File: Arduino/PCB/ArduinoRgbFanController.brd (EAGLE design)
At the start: 100 x 100 mm, 53 parts, among them IC2 ARDUINO_MKRFOX1200PROTOPADS, Q1 MOSFET-PCHANNEL, Q2 MOSFET-NCHANNELAO3404A

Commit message: Tidied up schematic.
Added values to resistors.
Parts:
- R10, R7, R8, R9: value (none) -> 10k
- R2, R20, R3, R4, R6: value (none) -> 100k
- R21: value (none) -> 10R
- R28: value (none) -> 300R
- R5: value (none) -> 00k
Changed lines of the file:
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@@
 </element>
 <element name="IC2" library="Arduino" package="ARDUINO_MKRFOX1200_PROTOPADS" value="ARDUINO_MKRFOX1200PROTOPADS" x="37.465" y="30.7975"/>
-<element name="R28" library="SparkFun-Resistors" package="1206" value="" x="81.5975" y="56.515" smashed="yes" rot="R180">
+<element name="R28" library="SparkFun-Resistors" package="1206" value="300R" x="81.5975" y="56.515" smashed="yes" rot="R180">
 <attribute name="VALUE" x="82.9945" y="58.039" size="0.4064" layer="27" rot="R180"/>
 </element>
@@
 <attribute name="VALUE" x="91.821" y="11.6205" size="0.4064" layer="27" rot="R180"/>
 </element>
-<element name="R20" library="SparkFun-Resistors" package="1206" value="" x="86.36" y="10.795" smashed="yes" rot="R90">
+<element name="R20" library="SparkFun-Resistors" package="1206" value="100k" x="86.36" y="10.795" smashed="yes" rot="R90">
 <attribute name="NAME" x="85.4075" y="13.5255" size="1.016" layer="25"/>
 <attribute name="VALUE" x="87.884" y="9.398" size="0.4064" layer="27" rot="R90"/>
 </element>
-<element name="R21" library="SparkFun-Resistors" package="1206" value="" x="95.885" y="11.43" smashed="yes">
+<element name="R21" library="SparkFun-Resistors" package="1206" value="10R" x="95.885" y="11.43" smashed="yes">
 <attribute name="NAME" x="95.25" y="12.8905" size="1.016" layer="25"/>
 <attribute name="VALUE" x="94.488" y="9.906" size="0.4064" layer="27"/>
@@
 <attribute name="VALUE" x="15.875" y="51.435" size="1.27" layer="27" rot="R270"/>
 </element>
-<element name="R2" library="SparkFun-Resistors" package="1206" value="" x="15.24" y="43.18" smashed="yes" rot="R180">
+<element name="R2" library="SparkFun-Resistors" package="1206" value="100k" x="15.24" y="43.18" smashed="yes" rot="R180">
 <attribute name="NAME" x="13.0175" y="44.6405" size="1.016" layer="25"/>
 <attribute name="VALUE" x="16.637" y="44.704" size="0.4064" layer="27" rot="R180"/>
 </element>
-<element name="R3" library="SparkFun-Resistors" package="1206" value="" x="15.24" y="27.94" smashed="yes" rot="R180">
+<element name="R3" library="SparkFun-Resistors" package="1206" value="100k" x="15.24" y="27.94" smashed="yes" rot="R180">
 <attribute name="NAME" x="13.0175" y="29.4005" size="1.016" layer="25"/>
 <attribute name="VALUE" x="16.637" y="29.464" size="0.4064" layer="27" rot="R180"/>
 </element>
-<element name="R4" library="SparkFun-Resistors" package="1206" value="" x="85.725" y="46.99" smashed="yes">
+<element name="R4" library="SparkFun-Resistors" package="1206" value="100k" x="85.725" y="46.99" smashed="yes">
 <attribute name="NAME" x="84.455" y="48.133" size="1.016" layer="25"/>
 <attribute name="VALUE" x="84.328" y="45.466" size="0.4064" layer="27"/>
 </element>
-<element name="R5" library="SparkFun-Resistors" package="1206" value="" x="85.725" y="25.4" smashed="yes">
+<element name="R5" library="SparkFun-Resistors" package="1206" value="00k" x="85.725" y="25.4" smashed="yes">
 <attribute name="NAME" x="83.5025" y="26.8605" size="1.016" layer="25"/>
 <attribute name="VALUE" x="84.328" y="23.876" size="0.4064" layer="27"/>
 </element>
-<element name="R6" library="SparkFun-Resistors" package="1206" value="" x="75.565" y="10.795" smashed="yes" rot="R270">
+<element name="R6" library="SparkFun-Resistors" package="1206" value="100k" x="75.565" y="10.795" smashed="yes" rot="R270">
 <attribute name="NAME" x="74.6125" y="7.1755" size="1.016" layer="25"/>
 <attribute name="VALUE" x="74.041" y="12.192" size="0.4064" layer="27" rot="R270"/>
 </element>
-<element name="R7" library="SparkFun-Resistors" package="1206" value="" x="85.725" y="32.385" smashed="yes" rot="R180">
+<element name="R7" library="SparkFun-Resistors" package="1206" value="10k" x="85.725" y="32.385" smashed="yes" rot="R180">
 <attribute name="NAME" x="83.82" y="34.163" size="1.016" layer="25"/>
 <attribute name="VALUE" x="87.122" y="33.909" size="0.4064" layer="27" rot="R180"/>
 </element>
-<element name="R8" library="SparkFun-Resistors" package="1206" value="" x="85.725" y="37.465" smashed="yes" rot="R180">
+<element name="R8" library="SparkFun-Resistors" package="1206" value="10k" x="85.725" y="37.465" smashed="yes" rot="R180">
 <attribute name="NAME" x="83.5025" y="38.9255" size="1.016" layer="25"/>
 <attribute name="VALUE" x="87.122" y="38.989" size="0.4064" layer="27" rot="R180"/>
 </element>
-<element name="R9" library="SparkFun-Resistors" package="1206" value="" x="15.24" y="20.32" smashed="yes">
+<element name="R9" library="SparkFun-Resistors" package="1206" value="10k" x="15.24" y="20.32" smashed="yes">
 <attribute name="NAME" x="13.0175" y="21.7805" size="1.016" layer="25"/>
 <attribute name="VALUE" x="13.843" y="18.796" size="0.4064" layer="27"/>
 </element>
-<element name="R10" library="SparkFun-Resistors" package="1206" value="" x="15.24" y="34.925" smashed="yes">
+<element name="R10" library="SparkFun-Resistors" package="1206" value="10k" x="15.24" y="34.925" smashed="yes">
 <attribute name="NAME" x="13.0175" y="36.3855" size="1.016" layer="25"/>
 <attribute name="VALUE" x="13.843" y="33.401" size="0.4064" layer="27"/>

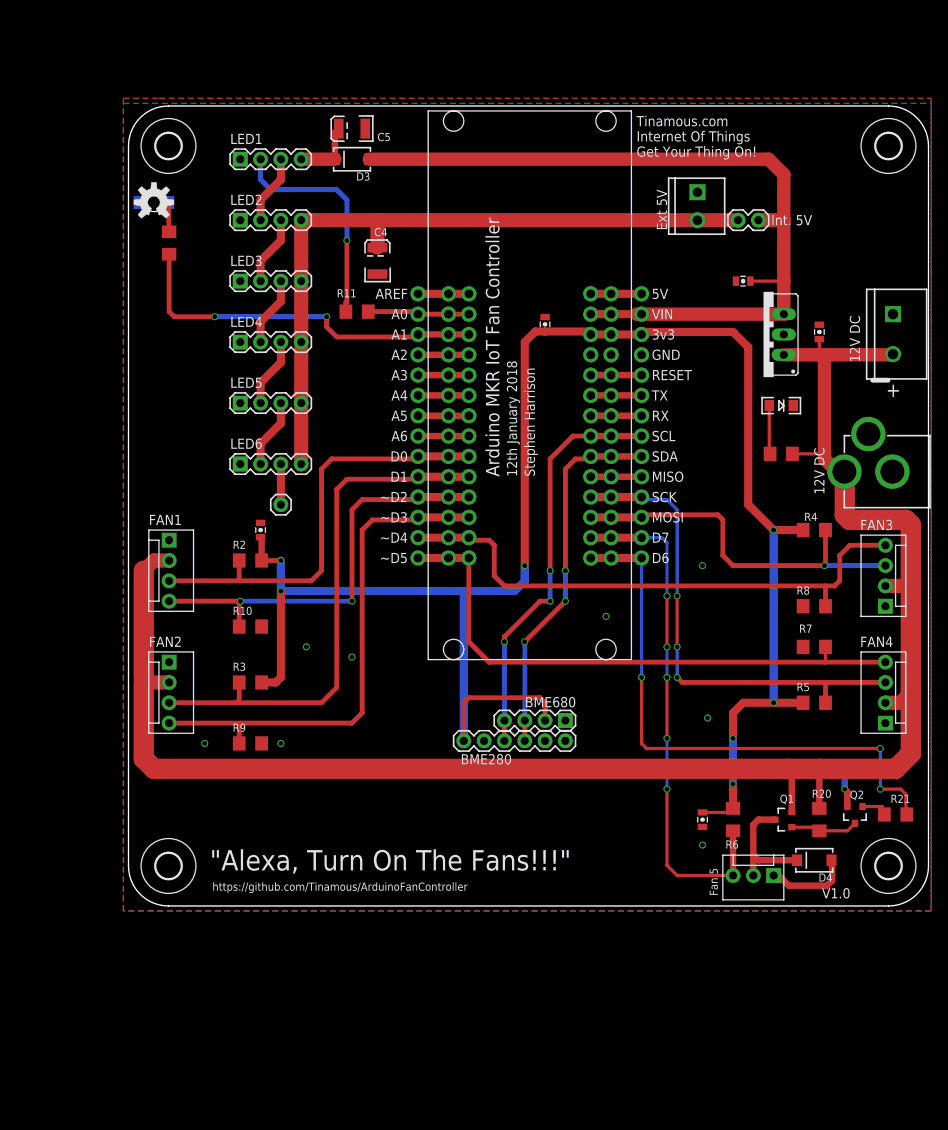
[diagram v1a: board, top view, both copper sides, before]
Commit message: Updated to add dust sensor and switch/led drivers. Updated files at DirtyPCBs
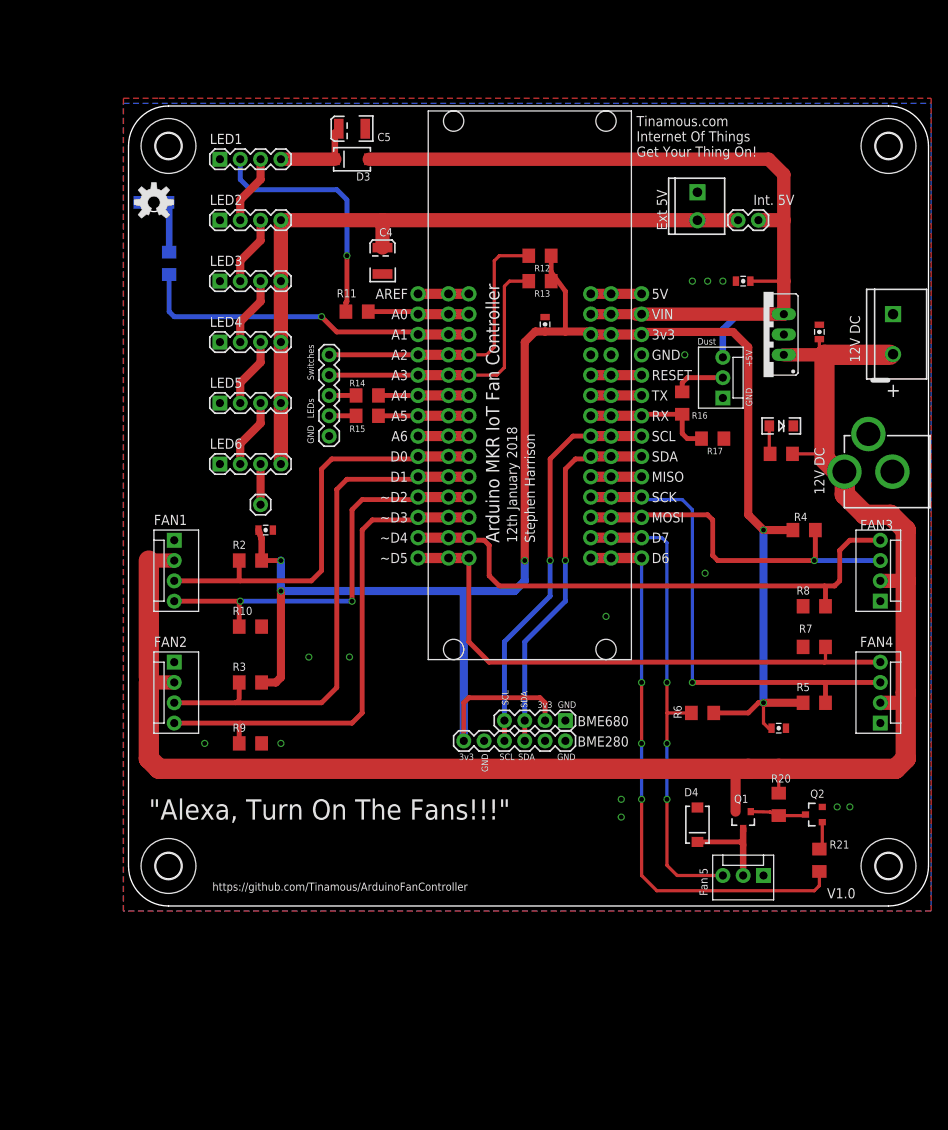
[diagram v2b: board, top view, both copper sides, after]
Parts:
- added JP3: (no value), SparkFun-Connectors:1X05
- added JP5: (no value), SparkFun-Connectors:MOLEX-1X3
- added R12, R13: 100k, SparkFun-Resistors:1206
- added R14, R15: 100R, SparkFun-Resistors:1206
- added R16: 10k, SparkFun-Resistors:1206
- added R17: 16k, SparkFun-Resistors:1206
- R5: value 00k -> 100k
- moved D4 15.3 mm to (71.1, 10.2), turned to 270 degrees
- moved C6 14.9 mm to (81.3, 22.2), turned to 0 degrees
- moved R6 13.9 mm to (71.8, 24.1), turned to 180 degrees
- moved R21 11.1 mm to (86.4, 5.71), turned to 270 degrees
- moved R20 5.43 mm to (81.3, 12.7)
- moved Q1 5.08 mm to (76.8, 10.8), turned to 180 degrees
- moved Q2 5.08 mm to (85.7, 11.4), turned to 90 degrees
- moved R1 2.54 mm to (5.08, 80.3), flipped to the bottom
- moved JP15 2.54 mm to (11.4, 93.3)
- moved JP25 2.54 mm to (11.4, 85.7)
- moved JP31 2.54 mm to (11.4, 78.1)
- moved JP34 2.54 mm to (11.4, 70.5)
- moved JP36 2.54 mm to (11.4, 62.9)
- moved JP37 2.54 mm to (11.4, 55.2)
- moved D2 2.54 mm to (81.6, 60.0)
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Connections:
- net A6C renamed SWITCH_ENABLE
- removed net A2C: IC2.#A2, IC2.@A2, IC2.A2
- removed net A3C: IC2.#A3, IC2.@A3, IC2.A3
- removed net A4C: IC2.#A4, IC2.@A4, IC2.A4
- removed net A5C: IC2.#A5, IC2.@A5, IC2.A5
- new net LED1: IC2.#A4, IC2.@A4, IC2.A4, R14.2
- new net LED2: IC2.#A5, IC2.@A5, IC2.A5, R15.2
- new net N$3: JP3.3, R14.1
- new net N$4: JP3.2, R15.1
- new net N$7: JP5.2, R16.2
- new net SWITCH1: IC2.#A2, IC2.@A2, IC2.A2, JP3.5, R12.2
- new net SWITCH2: IC2.#A3, IC2.@A3, IC2.A3, JP3.4, R13.2
- net 3.3V: now also R12.1, R13.1
- net GND: now also JP3.1, JP5.1, R17.1
- net RXC: now also R16.1, R17.2
- net VIN: now also JP5.3
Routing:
- net SWITCH1: track 0.00 -> 36.4 mm
- net SWITCH2: track 0.00 -> 35.8 mm
- net GND: track 14.2 -> 0.00 mm, vias 9 -> 14
- net VIN: track 102.2 -> 114.1 mm
- net LED2: track 0.00 -> 11.3 mm
- net LED1: track 0.00 -> 11.3 mm
- net RXC: track 6.35 -> 16.6 mm
- net N$7: track 0.00 -> 6.48 mm
- net A5C: track 6.35 -> 0.00 mm
- net A4C: track 6.35 -> 0.00 mm
- net A3C: track 6.35 -> 0.00 mm
- net A2C: track 6.35 -> 0.00 mm
- net 12V: track 224.5 -> 220.4 mm
- net FAN5_TACH: track 64.5 -> 60.7 mm, vias 5 -> 3
- net N$4: track 0.00 -> 3.36 mm
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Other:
- board text added: "+5V"
- board text added: "3v3"
- board text added: "A3 doesn't support interrupts, swap switch to A1."
- board text added: "D6 doesn't support PWM, doesn't matter as we want on/off only, so any pin can be used"
- board text added: "Dust"
- board text added: "GND"
- board text added: "LEDs"
- board text added: "PWM fans appear to run at min speed when 12V applied but low on PWM. Need P-Fet to kill the 12v"
- board text added: "RX doesn't support interrupts, swap switch to 6?."
- board text added: "SCL"
- board text added: "SDA"
- board text added: "Switches"

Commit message: Moved dust sensor connection to PCB edge.
Removed pullup/down resistors for PWM and tach signals as they are not needed.

Added P-FET + N-FET power control to switch the 12V to the PWM fans as some fans do not switch off when PWM off.

Moved 12V LED to switched fan power line and to underneath the "On" lettering.
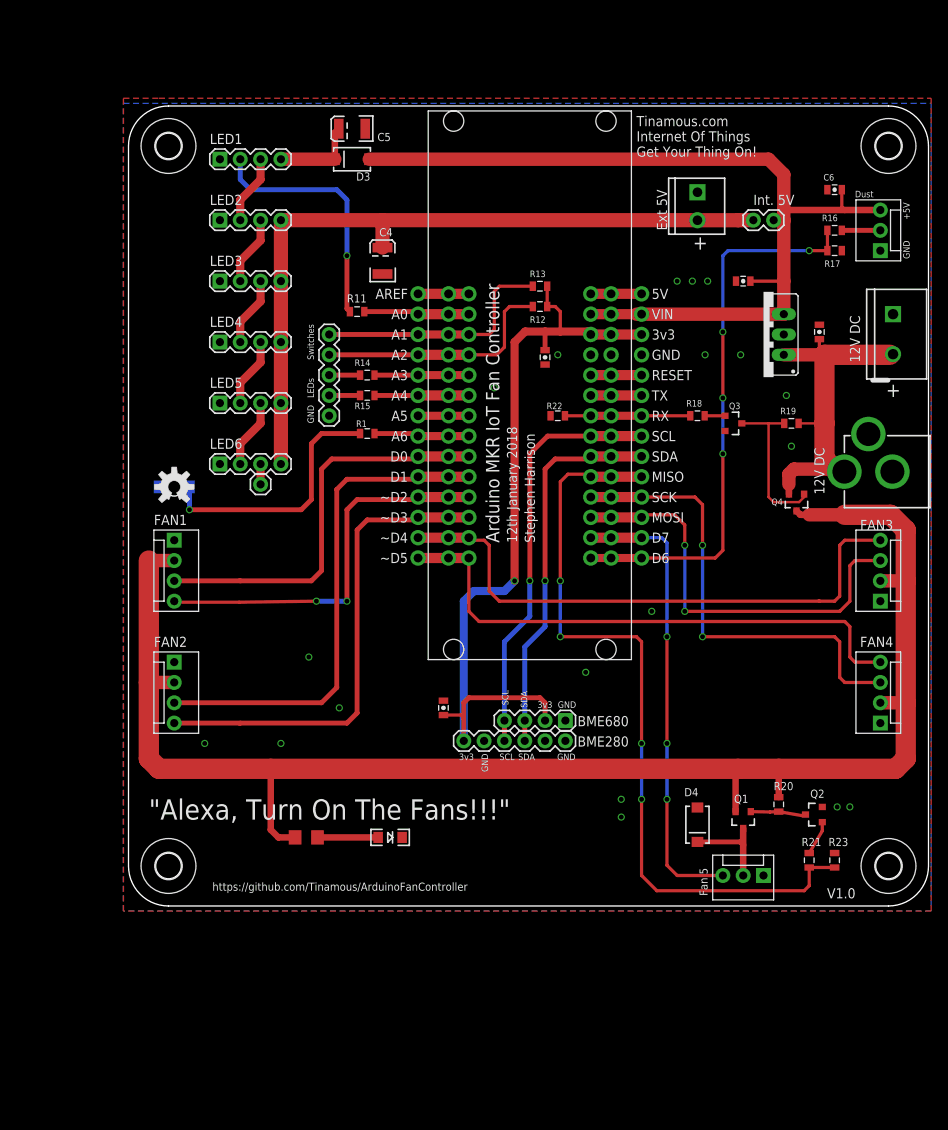
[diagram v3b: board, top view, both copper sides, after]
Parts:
- removed R10, R7, R8, R9: 10k, SparkFun-Resistors:1206
- removed R2, R3, R4, R5, R6: 100k, SparkFun-Resistors:1206
- added Q3: 2N7002, SparkFun-DiscreteSemi:SOT23-3
- added Q4: IRLML9301TRPBF, SparkFun-DiscreteSemi:SOT23-3
- added R18: 10R, SparkFun-Resistors:0805
- added R19: 100k, SparkFun-Resistors:0805
- added R22, R23: 1M, SparkFun-Resistors:0805
- Q1: value MOSFET-PCHANNEL -> IRLML9301TRPBF
- Q2: value MOSFET-NCHANNELAO3404A -> 2N7002
- R1, R11, R12, R13, R14, R15, R16, R17, R20, R21: device SparkFun-Resistors:1206 -> SparkFun-Resistors:0805
- moved R28 76.3 mm to (22.2, 8.57), turned to 0 degrees
- moved D2 71.0 mm to (32.7, 8.57)
- moved C6 67.7 mm to (88.3, 89.5), turned to 180 degrees
- moved D1 35.7 mm to (5.71, 52.4)
- moved LOGO3 35.7 mm to (5.71, 52.4)
- moved R1 32.6 mm to (29.8, 59.1), flipped to the top, turned to 0 degrees
- moved C7 31.4 mm to (39.4, 24.8), turned to 90 degrees
- moved R16 28.8 mm to (88.3, 84.5), turned to 0 degrees
- moved R17 28.0 mm to (88.3, 81.9)
- moved JP5 27.0 mm to (94.0, 81.9)
- moved R12 6.35 mm to (51.4, 74.9)
- moved R15 5.08 mm to (29.8, 66.4)
- moved C3 4.13 mm to (52.1, 68.6), turned to 270 degrees
- moved JP3 2.54 mm to (25.1, 61.3)
- moved JP38 2.54 mm to (16.5, 52.7)
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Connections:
- removed net MISO: IC2.#MISO, IC2.@MISO, IC2.MISO
- removed net RXC: IC2.#RX, IC2.@RX, IC2.RX, R16.1, R17.2
- removed net SWITCH_ENABLE: IC2.#A6, IC2.@A6, IC2.A6
- new net DUST_SENSOR: IC2.#D6, IC2.@D6, IC2.D6, R16.1, R17.2
- new net FAN_POWER: JP13.2, JP6.2, JP8.2, JP9.2, Q1.2, Q4.3, R20.2, R28.1
- new net FAN_POWER_CONTROL: IC2.#RX, IC2.@RX, IC2.RX, R18.2, R22.1
- new net N$5: Q3.3, Q4.1, R19.2
- new net N$6: Q3.1, R18.1
- new net SWITCH_ENABLED: IC2.#A5, IC2.@A5, IC2.A5
- net 12V: now also Q4.2, R19.1; no longer JP13.2, JP6.2, JP8.2, JP9.2, Q1.2, R20.2, R28.1
- net 3.3V: no longer C6.1, R2.1, R3.1, R4.1, R5.1, R6.1
- net FAN1_PWM: no longer R10.1
- net FAN1_TACH: no longer R2.2
- net FAN2_PWM: no longer R9.1
- net FAN2_TACH: no longer R3.2
- net FAN3_PWM: no longer R8.1
- net FAN3_TACH: no longer R4.2
- net FAN4_PWM: no longer R7.1
- net FAN4_TACH: no longer R5.2
- net FAN5_PWM: now also IC2.#MISO, IC2.@MISO, IC2.MISO, R23.1; no longer IC2.#D6, IC2.@D6, IC2.D6
- net FAN5_TACH: no longer R6.2
- net GND: now also Q3.2, R22.2, R23.2; no longer R10.2, R7.2, R8.2, R9.2
- net LED2: now also IC2.#A3, IC2.@A3, IC2.A3; no longer IC2.#A5, IC2.@A5, IC2.A5
- net N$3: now also JP3.2; no longer JP3.3
- net N$4: now also JP3.3; no longer JP3.2
- net OSH_LED: now also IC2.#A6, IC2.@A6, IC2.A6; no longer IC2.#A1, IC2.@A1, IC2.A1
- net SWITCH1: now also JP3.4; no longer JP3.5
- net SWITCH2: now also IC2.#A1, IC2.@A1, IC2.A1, JP3.5; no longer IC2.#A3, IC2.@A3, IC2.A3, JP3.4
- net VIN: now also C6.1
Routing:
- net FAN_POWER: track 0.00 -> 196.4 mm
- net 12V: track 220.4 -> 45.4 mm
- net 3.3V: track 226.0 -> 101.4 mm, vias 5 -> 1
- net DUST_SENSOR: track 0.00 -> 70.1 mm, vias 0 -> 4
- net OSH_LED: track 44.6 -> 11.9 mm, vias 1 -> 0
- net FAN5_PWM: track 71.1 -> 97.1 mm, vias 3 -> 4
- net N$1: track 6.26 -> 32.3 mm, vias 0 -> 1
- net N$5: track 0.00 -> 19.8 mm
- net RXC: track 16.6 -> 0.00 mm
- net FAN_POWER_CONTROL: track 0.00 -> 15.7 mm
- net FAN3_TACH: track 45.2 -> 60.3 mm, vias 1 -> 2
- net MISO: track 6.35 -> 0.00 mm
- net SWITCH_ENABLED: track 0.00 -> 6.35 mm
- net SWITCH_ENABLE: track 6.35 -> 0.00 mm
- net SWITCH1: track 36.4 -> 30.6 mm
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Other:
- board text removed: "A3 doesn't support interrupts, swap switch to A1."
- board text removed: "D6 doesn't support PWM, doesn't matter as we want on/off only, so any pin can be used"
- board text removed: "PWM fans appear to run at min speed when 12V applied but low on PWM. Need P-Fet to kill the 12v"
- board text removed: "RX doesn't support interrupts, swap switch to 6?."
